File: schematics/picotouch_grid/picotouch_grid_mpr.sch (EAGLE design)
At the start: 188 parts, among them J1 AUDIO-JACK-TRRS, J2 AUDIO-JACK-TRRS, J3 AUDIO-JACK-TRRS, J4 STEMMA_I2C_QT, K1 TOUCHKEYH, K10 TOUCHKEYH, K11 TOUCHKEYH, K12 TOUCHKEYH, K13 TOUCHKEYH, K14 TOUCHKEYH, K15 TOUCHKEYH, K16 TOUCHKEYH, K17 TOUCHKEYH, K18 TOUCHKEYH, K19 TOUCHKEYH, K2 TOUCHKEYH, K20 TOUCHKEYH, K21 TOUCHKEYH, K22 TOUCHKEYH, K23 TOUCHKEYH, K24 TOUCHKEYH, K25 TOUCHKEYH, K26 TOUCHKEYH, K27 TOUCHKEYH, K28 TOUCHKEYH, K29 TOUCHKEYH, K3 TOUCHKEYH, K30 TOUCHKEYH, K31 TOUCHKEYH, K32 TOUCHKEYH, K33 TOUCHKEYH, K34 TOUCHKEYH, K35 TOUCHKEYH, K36 TOUCHKEYH, K37 TOUCHKEYH, K38 TOUCHKEYH, K39 TOUCHKEYH, K4 TOUCHKEYH, K40 TOUCHKEYH, K5 TOUCHKEYH, K6 TOUCHKEYH, K7 TOUCHKEYH, K8 TOUCHKEYH, K9 TOUCHKEYH, U1 RASPBERRY_PICO, U2 MPR121, U3 MPR121, U4 MPR121, U5 MPR121, U6 H11L1MS, U7 ADAFRUIT_QTPY_BFF

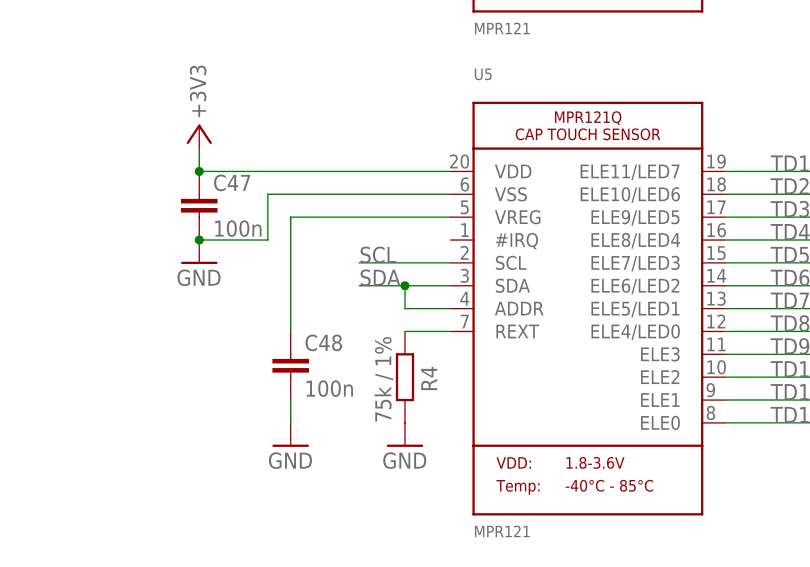
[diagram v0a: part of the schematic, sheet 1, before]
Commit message: move confusing research code to research dir
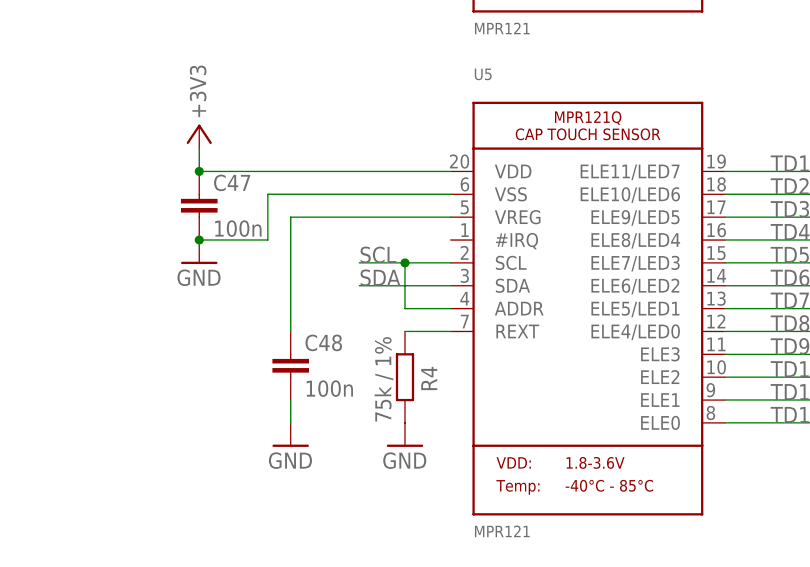
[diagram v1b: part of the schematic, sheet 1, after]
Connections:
- net SCL: now also U5.ADDR
- net SDA: no longer U5.ADDR
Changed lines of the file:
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@@
 <grid distance="0.1" unitdist="inch" unit="inch" style="lines" multiple="1" display="no" altdistance="0.01" altunitdist="inch" altunit="inch"/>
 <layers>
-<layer number="1" name="Top" color="4" fill="1" visible="yes" active="no"/>
-<layer number="2" name="Route2" color="16" fill="1" visible="yes" active="no"/>
-<layer number="3" name="Route3" color="17" fill="1" visible="yes" active="no"/>
-<layer number="4" name="Route4" color="18" fill="1" visible="yes" active="no"/>
-<layer number="5" name="Route5" color="19" fill="1" visible="yes" active="no"/>
-<layer number="6" name="Route6" color="25" fill="1" visible="yes" active="no"/>
-<layer number="7" name="Route7" color="26" fill="1" visible="yes" active="no"/>
-<layer number="8" name="Route8" color="27" fill="1" visible="yes" active="no"/>
-<layer number="9" name="Route9" color="28" fill="1" visible="yes" active="no"/>
-<layer number="10" name="Route10" color="29" fill="1" visible="yes" active="no"/>
-<layer number="11" name="Route11" color="30" fill="1" visible="yes" active="no"/>
-<layer number="12" name="Route12" color="20" fill="1" visible="yes" active="no"/>
-<layer number="13" name="Route13" color="21" fill="1" visible="yes" active="no"/>
-<layer number="14" name="Route14" color="22" fill="1" visible="yes" active="no"/>
-<layer number="15" name="Route15" color="23" fill="1" visible="yes" active="no"/>
-<layer number="16" name="Bottom" color="1" fill="1" visible="yes" active="no"/>
-<layer number="17" name="Pads" color="2" fill="1" visible="yes" active="no"/>
-<layer number="18" name="Vias" color="2" fill="1" visible="yes" active="no"/>
-<layer number="19" name="Unrouted" color="6" fill="1" visible="yes" active="no"/>
-<layer number="20" name="Dimension" color="15" fill="1" visible="yes" active="no"/>
-<layer number="21" name="tPlace" color="15" fill="1" visible="yes" active="no"/>
-<layer number="22" name="bPlace" color="15" fill="1" visible="yes" active="no"/>
-<layer number="23" name="tOrigins" color="15" fill="1" visible="yes" active="no"/>
-<layer number="24" name="bOrigins" color="15" fill="1" visible="yes" active="no"/>
-<layer number="25" name="tNames" color="15" fill="1" visible="yes" active="no"/>
-<layer number="26" name="bNames" color="15" fill="1" visible="yes" active="no"/>
-<layer number="27" name="tValues" color="15" fill="1" visible="yes" active="no"/>
-<layer number="28" name="bValues" color="15" fill="1" visible="yes" active="no"/>
+<layer number="1" name="Top" color="4" fill="1" visible="no" active="no"/>
+<layer number="2" name="Route2" color="16" fill="1" visible="no" active="no"/>
+<layer number="3" name="Route3" color="17" fill="1" visible="no" active="no"/>
+<layer number="4" name="Route4" color="18" fill="1" visible="no" active="no"/>
+<layer number="5" name="Route5" color="19" fill="1" visible="no" active="no"/>
+<layer number="6" name="Route6" color="25" fill="1" visible="no" active="no"/>
+<layer number="7" name="Route7" color="26" fill="1" visible="no" active="no"/>
+<layer number="8" name="Route8" color="27" fill="1" visible="no" active="no"/>
+<layer number="9" name="Route9" color="28" fill="1" visible="no" active="no"/>
+<layer number="10" name="Route10" color="29" fill="1" visible="no" active="no"/>
+<layer number="11" name="Route11" color="30" fill="1" visible="no" active="no"/>
+<layer number="12" name="Route12" color="20" fill="1" visible="no" active="no"/>
+<layer number="13" name="Route13" color="21" fill="1" visible="no" active="no"/>
+<layer number="14" name="Route14" color="22" fill="1" visible="no" active="no"/>
+<layer number="15" name="Route15" color="23" fill="1" visible="no" active="no"/>
+<layer number="16" name="Bottom" color="1" fill="1" visible="no" active="no"/>
+<layer number="17" name="Pads" color="2" fill="1" visible="no" active="no"/>
+<layer number="18" name="Vias" color="2" fill="1" visible="no" active="no"/>
+<layer number="19" name="Unrouted" color="6" fill="1" visible="no" active="no"/>
+<layer number="20" name="Dimension" color="15" fill="1" visible="no" active="no"/>
+<layer number="21" name="tPlace" color="15" fill="1" visible="no" active="no"/>
+<layer number="22" name="bPlace" color="15" fill="1" visible="no" active="no"/>
+<layer number="23" name="tOrigins" color="15" fill="1" visible="no" active="no"/>
+<layer number="24" name="bOrigins" color="15" fill="1" visible="no" active="no"/>
+<layer number="25" name="tNames" color="15" fill="1" visible="no" active="no"/>
+<layer number="26" name="bNames" color="15" fill="1" visible="no" active="no"/>
+<layer number="27" name="tValues" color="15" fill="1" visible="no" active="no"/>
+<layer number="28" name="bValues" color="15" fill="1" visible="no" active="no"/>
 <layer number="29" name="tStop" color="7" fill="3" visible="no" active="no"/>
 <layer number="30" name="bStop" color="7" fill="6" visible="no" active="no"/>
@@
 <layer number="35" name="tGlue" color="7" fill="4" visible="no" active="no"/>
 <layer number="36" name="bGlue" color="7" fill="5" visible="no" active="no"/>
-<layer number="37" name="tTest" color="7" fill="1" visible="yes" active="no"/>
-<layer number="38" name="bTest" color="7" fill="1" visible="yes" active="no"/>
+<layer number="37" name="tTest" color="7" fill="1" visible="no" active="no"/>
+<layer number="38" name="bTest" color="7" fill="1" visible="no" active="no"/>
 <layer number="39" name="tKeepout" color="4" fill="11" visible="no" active="no"/>
 <layer number="40" name="bKeepout" color="1" fill="11" visible="no" active="no"/>
@@
 <layer number="44" name="Drills" color="7" fill="1" visible="no" active="no"/>
 <layer number="45" name="Holes" color="7" fill="1" visible="no" active="no"/>
-<layer number="46" name="Milling" color="3" fill="1" visible="yes" active="no"/>
-<layer number="47" name="Measures" color="7" fill="1" visible="yes" active="no"/>
-<layer number="48" name="Document" color="15" fill="1" visible="yes" active="no"/>
-<layer number="49" name="Reference" color="15" fill="1" visible="yes" active="no"/>
-<layer number="50" name="dxf" color="7" fill="1" visible="yes" active="no"/>
-<layer number="51" name="tDocu" color="15" fill="1" visible="yes" active="no"/>
-<layer number="52" name="bDocu" color="15" fill="1" visible="yes" active="no"/>
-<layer number="53" name="tGND_GNDA" color="7" fill="9" visible="yes" active="no"/>
-<layer number="54" name="bGND_GNDA" color="1" fill="9" visible="yes" active="no"/>
-<layer number="56" name="wert" color="7" fill="1" visible="yes" active="no"/>
-<layer number="57" name="tCAD" color="7" fill="1" visible="yes" active="no"/>
-<layer number="58" name="b3D" color="7" fill="1" visible="yes" active="no"/>
-<layer number="59" name="tCarbon" color="7" fill="1" visible="yes" active="no"/>
-<layer number="60" name="bCarbon" color="7" fill="1" visible="yes" active="no"/>
-<layer number="61" name="stand" color="7" fill="1" visible="yes" active="no"/>
+<layer number="46" name="Milling" color="3" fill="1" visible="no" active="no"/>
+<layer number="47" name="Measures" color="7" fill="1" visible="no" active="no"/>
+<layer number="48" name="Document" color="15" fill="1" visible="no" active="no"/>
+<layer number="49" name="Reference" color="15" fill="1" visible="no" active="no"/>
+<layer number="50" name="dxf" color="7" fill="1" visible="no" active="no"/>
+<layer number="51" name="tDocu" color="15" fill="1" visible="no" active="no"/>
+<layer number="52" name="bDocu" color="15" fill="1" visible="no" active="no"/>
+<layer number="53" name="tGND_GNDA" color="7" fill="9" visible="no" active="no"/>
+<layer number="54" name="bGND_GNDA" color="1" fill="9" visible="no" active="no"/>
+<layer number="56" name="wert" color="7" fill="1" visible="no" active="no"/>
+<layer number="57" name="tCAD" color="7" fill="1" visible="no" active="no"/>
+<layer number="58" name="b3D" color="7" fill="1" visible="no" active="no"/>
+<layer number="59" name="tCarbon" color="7" fill="1" visible="no" active="no"/>
+<layer number="60" name="bCarbon" color="7" fill="1" visible="no" active="no"/>
+<layer number="61" name="stand" color="7" fill="1" visible="no" active="no"/>
 <layer number="88" name="SimResults" color="9" fill="1" visible="yes" active="yes"/>
 <layer number="89" name="SimProbes" color="9" fill="1" visible="yes" active="yes"/>
@@
 <segment>
 <pinref part="U5" gate="G$1" pin="SCL"/>
-<wire x1="452.12" y1="60.96" x2="441.96" y2="60.96" width="0.1524" layer="91"/>
+<wire x1="452.12" y1="60.96" x2="447.04" y2="60.96" width="0.1524" layer="91"/>
 <label x="441.96" y="60.96" size="1.778" layer="95"/>
+<pinref part="U5" gate="G$1" pin="ADDR"/>
+<wire x1="447.04" y1="60.96" x2="441.96" y2="60.96" width="0.1524" layer="91"/>
+<wire x1="447.04" y1="55.88" x2="452.12" y2="55.88" width="0.1524" layer="91"/>
+<wire x1="447.04" y1="60.96" x2="447.04" y2="55.88" width="0.1524" layer="91"/>
+<junction x="447.04" y="60.96"/>
 </segment>
 </net>
@@
 </segment>
 <segment>
-<pinref part="U5" gate="G$1" pin="ADDR"/>
-<wire x1="447.04" y1="55.88" x2="452.12" y2="55.88" width="0.1524" layer="91"/>
 <pinref part="U5" gate="G$1" pin="SDA"/>
-<wire x1="452.12" y1="58.42" x2="447.04" y2="58.42" width="0.1524" layer="91"/>
-<wire x1="447.04" y1="58.42" x2="441.96" y2="58.42" width="0.1524" layer="91"/>
-<wire x1="447.04" y1="55.88" x2="447.04" y2="58.42" width="0.1524" layer="91"/>
-<junction x="447.04" y="58.42"/>
+<wire x1="452.12" y1="58.42" x2="441.96" y2="58.42" width="0.1524" layer="91"/>
 <label x="441.96" y="58.42" size="1.778" layer="95"/>
 </segment>
